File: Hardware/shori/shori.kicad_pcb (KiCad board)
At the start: 4 copper layers, 101.5 x 44.8 mm, 137 parts, among them U1 CS4272, U2 STM32H750VBTx, U3 NE5532, U4 NE5532, U5 TPS73733DCQR, U6 W25Q128JVS, U7 TLV9001IDCK, Y1 12.288MHz

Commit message: added stiching vias on gen and changed SWD header on shori to header pins
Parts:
- removed R40: 10Ω, Resistor_SMD:R_0402_1005Metric_Pad0.72x0.64mm_HandSolder
- C15: value 47uF -> 100uF
- J2: renamed from PROGRAMMING; footprint Connector_Molex:Molex_PicoBlade_53048-0510_1x05_P1.25mm_Horizontal -> Connector_PinHeader_2.54mm:PinHeader_1x05_P2.54mm_Vertical
- J3: renamed from UART; footprint MyFootprints:CONN04_530480410_MOL -> MyFootprints:MOLEX_530480310
- J4: renamed from AUDIO IN
- J5: renamed from AUX IN
- J6: renamed from AUDIO OUT
- moved J2 3.98 mm to (130.6, 94.0), turned to -90 degrees
- moved D2 0.11 mm to (120.3, 98.8)
- renumbered POWER to J1, RST to RST1, B to SW1, 3.3V to TP2, 5VA to TP4, TX to TP6
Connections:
- C15 pad 1: +5VA -> +5V
- C24 pad 1: +5VA -> +5V
- C49 pad 1: +5VA -> +5V
- C50 pad 2: +5VA -> +5V
- R4 pad 1: +5VA -> +5V
- TP4 pad 1: +5VA -> +5V
- U1 pad 20: +5VA -> +5V
- U2 pad 6: unconnected-(U2-VBAT-Pad6) -> +3.3V
- U3 pad 8: +5VA -> +5V
- U4 pad 8: +5VA -> +5V
- U7 pad 5: +5VA -> +5V
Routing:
- net +5V: track 29.7 -> 104.9 mm, vias 0 -> 4
- net +5VA: track 73.8 -> 0.00 mm, vias 4 -> 0
- net +3.3V: track 162.4 -> 174.1 mm
- net /SWDIO: track 11.8 -> 14.5 mm
- net /NRST: track 67.9 -> 70.1 mm
- net /SWCLK: track 6.42 -> 8.41 mm
- net GND: track 93.0 -> 94.8 mm, vias 158 -> 156
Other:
- board text added: "This will give you the tone but not the skills"
- board text removed: "This will give you the tone But not the skills"

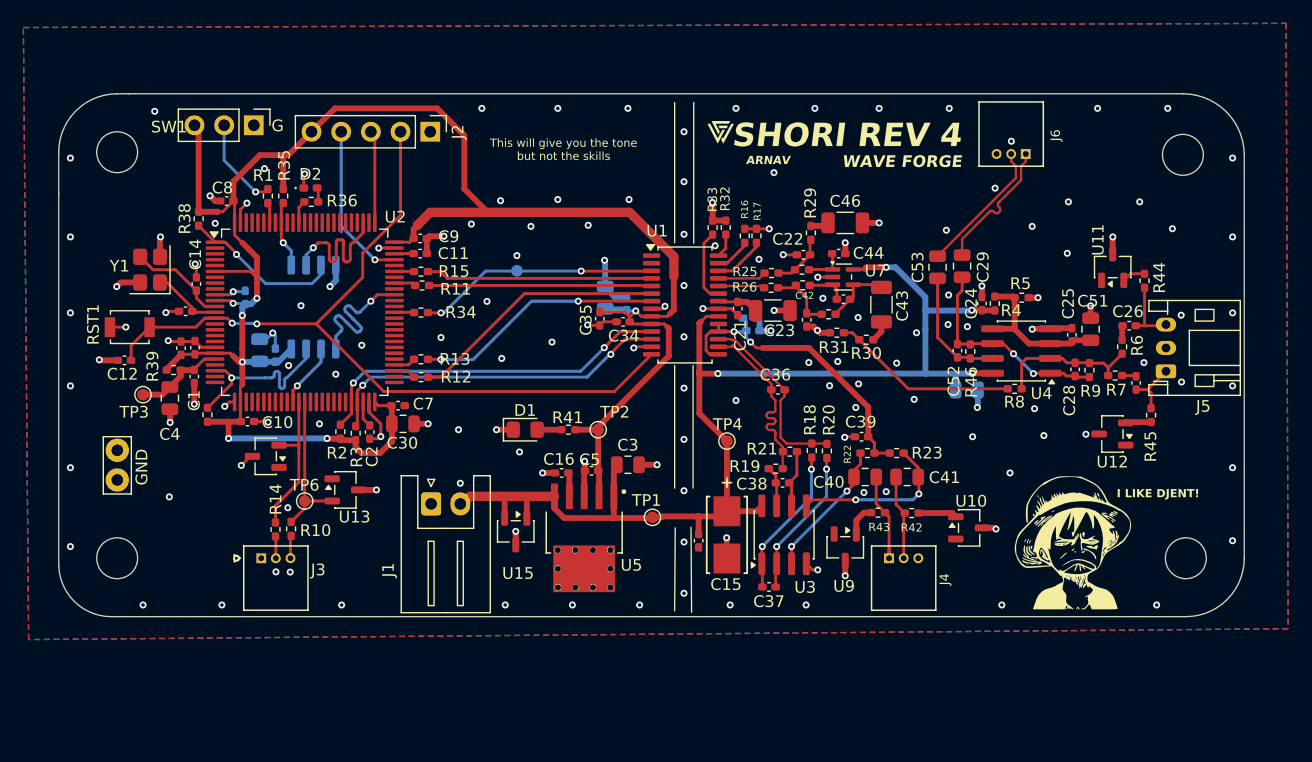
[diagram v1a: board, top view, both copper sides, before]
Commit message: Gen rev 2 Ordered and Assembled. Proven Working All rails Spot on
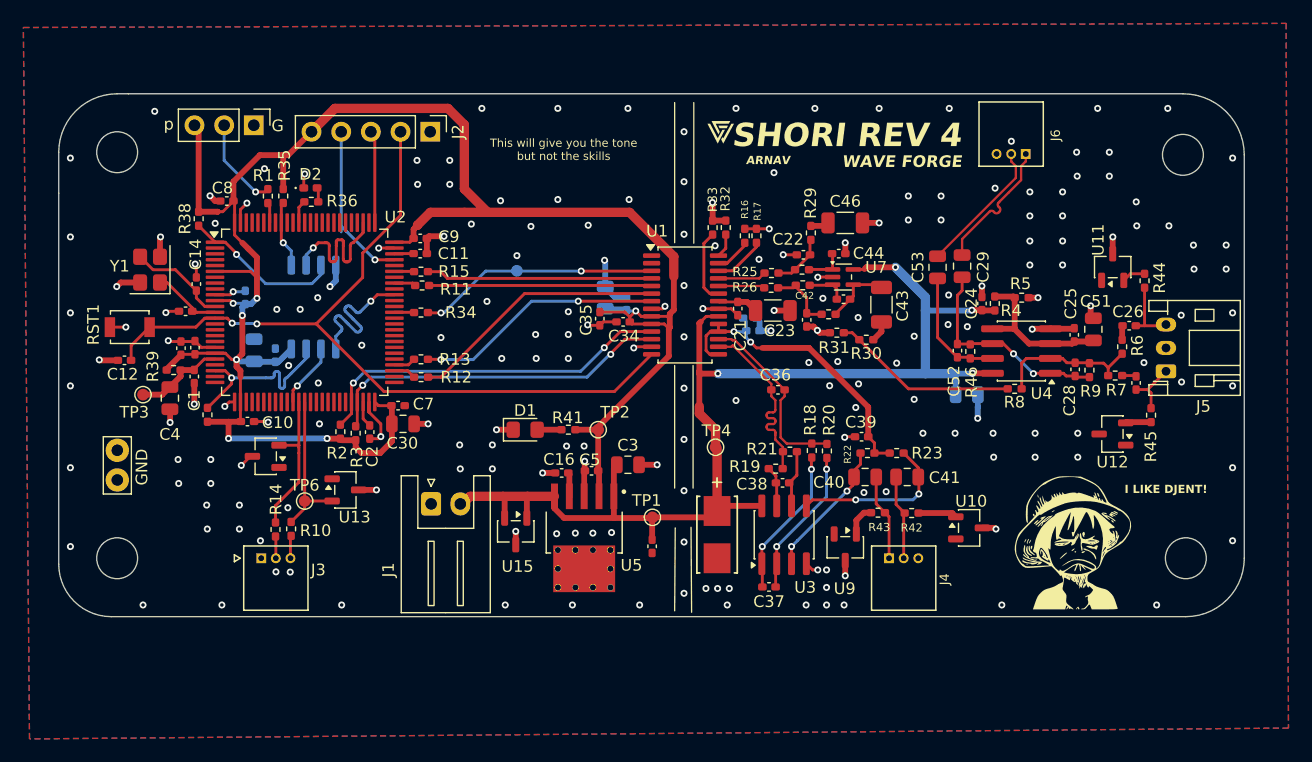
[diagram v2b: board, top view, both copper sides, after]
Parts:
- removed the G*** at (176.2, 112.1)
- moved C49 4.01 mm to (149.6, 129.5)
- moved TP4 1.11 mm to (155.0, 121.0)
- moved C15 0.84 mm to (155.1, 128.5)
- moved C47 0.49 mm to (115.5, 112.7)
- moved C50 0.40 mm to (176.5, 116.5)
- moved C51 0.23 mm to (187.3, 110.9)
- moved C25 0.20 mm to (185.7, 111.4)
- renumbered SW1 to p
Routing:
- net GND: track 94.8 -> 91.5 mm, vias 156 -> 204
- net +3.3V: track 174.1 -> 175.8 mm
- net /AUDIO_IN+: track 8.31 -> 7.41 mm
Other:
- board text removed: "John has mad guitar playing skills"
- board text removed: "John is awesome"
- board text removed: "This is John"
- board text removed: "You will never be like John"
